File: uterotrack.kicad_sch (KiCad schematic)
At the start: 77 parts, among them J1 RFShield, J2 MicroSD_Card, J3 Argos_Prog, J4 AS5510, J5 Prog, J6 EXP, Q1 DMP2110UW, Q10 MMBT2222, Q11 MMBT2222, Q12 MMBT2222, Q13 MMBT2222, Q2 DMP2110UW, Q3 MMBT2222, Q4 DMP2110UW, Q5 DMP2110UW, Q6 MMBT2222, Q7 SiS415DNT, Q8 DMP2110UW, Q9 MMBT2222, U1 Argos_SMD, U2 ESP32-S3-WROOM-1, U3 keller_6LHPD, U4 RV-3032-C7, U5 CAM-M8Q

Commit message: Change R38, R39, R43 and R44 to 0402
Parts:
- R15, R16, R17, R23, R24, R26, R27, R28, R30, R31, R32, R33, R34, R36, R37: manf# CRCW0402100KFKEDC -> CRCW0402100KFKED
- R19, R20, R21, R22, R25: manf# CRCW04024K70FKEDC -> CRCW04024K70FKED
- R29, R35: manf# CRCW040220K0FKEDC -> CRCW040220K0FKED
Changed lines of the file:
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@@
 			)
 		)
-		(property "manf#" "CRCW0402100KFKEDC"
+		(property "manf#" "CRCW0402100KFKED"
 			(at 64.77 246.38 0)
 			(effects
@@
 			)
 		)
-		(property "manf#" "CRCW0402100KFKEDC"
+		(property "manf#" "CRCW0402100KFKED"
 			(at 87.63 167.64 0)
 			(effects
@@
 			)
 		)
-		(property "manf#" "CRCW0402100KFKEDC"
+		(property "manf#" "CRCW0402100KFKED"
 			(at 83.82 156.21 0)
 			(effects
@@
 			)
 		)
-		(property "manf#" "CRCW0402100KFKEDC"
+		(property "manf#" "CRCW0402100KFKED"
 			(at 121.92 234.95 0)
 			(effects
@@
 			)
 		)
-		(property "manf#" "CRCW04024K70FKEDC"
+		(property "manf#" "CRCW04024K70FKED"
 			(at 62.23 157.48 0)
 			(effects
@@
 			)
 		)
-		(property "manf#" "CRCW040220K0FKEDC"
+		(property "manf#" "CRCW040220K0FKED"
 			(at 106.68 247.65 0)
 			(effects
@@
 			)
 		)
-		(property "manf#" "CRCW0402100KFKEDC"
+		(property "manf#" "CRCW0402100KFKED"
 			(at 93.98 173.99 0)
 			(effects
@@
 			)
 		)
-		(property "manf#" "CRCW04024K70FKEDC"
+		(property "manf#" "CRCW04024K70FKED"
 			(at 62.23 154.94 0)
 			(effects
@@
 			)
 		)
-		(property "manf#" "CRCW0402100KFKEDC"
+		(property "manf#" "CRCW0402100KFKED"
 			(at 60.96 234.95 0)
 			(effects
@@
 			)
 		)
-		(property "manf#" "CRCW0402100KFKEDC"
+		(property "manf#" "CRCW0402100KFKED"
 			(at 196.85 259.08 0)
 			(effects
@@
 			)
 		)
-		(property "manf#" "CRCW0402100KFKEDC"
+		(property "manf#" "CRCW0402100KFKED"
 			(at 125.73 246.38 0)
 			(effects
@@
 			)
 		)
-		(property "manf#" "CRCW0402100KFKEDC"
+		(property "manf#" "CRCW0402100KFKED"
 			(at 290.83 83.82 0)
 			(effects
@@
 			)
 		)
-		(property "manf#" "CRCW04024K70FKEDC"
+		(property "manf#" "CRCW04024K70FKED"
 			(at 105.41 111.76 0)
 			(effects
@@
 			)
 		)
-		(property "manf#" "CRCW0402100KFKEDC"
+		(property "manf#" "CRCW0402100KFKED"
 			(at 294.64 72.39 0)
 			(effects
@@
 			)
 		)
-		(property "manf#" "CRCW0402100KFKEDC"
+		(property "manf#" "CRCW0402100KFKED"
 			(at 129.54 156.21 0)
 			(effects
@@
 			)
 		)
-		(property "manf#" "CRCW0402100KFKEDC"
+		(property "manf#" "CRCW0402100KFKED"
 			(at 48.26 74.93 0)
 			(effects
@@
 			)
 		)
-		(property "manf#" "CRCW0402100KFKEDC"
+		(property "manf#" "CRCW0402100KFKED"
 			(at 71.12 252.73 0)
 			(effects
@@
 			)
 		)
-		(property "manf#" "CRCW04024K70FKEDC"
+		(property "manf#" "CRCW04024K70FKED"
 			(at 49.53 111.76 0)
 			(effects
@@
 			)
 		)
-		(property "manf#" "CRCW0402100KFKEDC"
+		(property "manf#" "CRCW0402100KFKED"
 			(at 201.93 243.84 0)
 			(effects
@@
 			)
 		)
-		(property "manf#" "CRCW040220K0FKEDC"
+		(property "manf#" "CRCW040220K0FKED"
 			(at 106.68 234.95 0)
 			(effects
@@
 			)
 		)
-		(property "manf#" "CRCW04024K70FKEDC"
+		(property "manf#" "CRCW04024K70FKED"
 			(at 49.53 109.22 0)
 			(effects
@@
 			)
 		)
-		(property "manf#" "CRCW0402100KFKEDC"
+		(property "manf#" "CRCW0402100KFKED"
 			(at 168.91 246.38 0)
 			(effects

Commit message: Change resistor of uSD and Argus PA to 0402
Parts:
- C4: footprint Capacitor_SMD:C_0603_1608Metric -> Capacitor_SMD:C_0402_1005Metric; manf# 0603YC104JAT2A -> CL05B104KO5NNNC
- R1, R2, R3, R4, R5, R8: footprint Resistor_SMD:R_0603_1608Metric -> Resistor_SMD:R_0402_1005Metric; manf# CRCW06030000Z0EAC -> CRCW04020000Z0ED
- R10, R11, R12, R13, R14, R18, R6, R7, R9: footprint Resistor_SMD:R_0603_1608Metric -> Resistor_SMD:R_0402_1005Metric; manf# CRCW060310K0FKEAC -> CRCW040210K0FKED
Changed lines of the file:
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@@
 			)
 		)
-		(property "Footprint" "Resistor_SMD:R_0603_1608Metric"
+		(property "Footprint" "Resistor_SMD:R_0402_1005Metric"
 			(at 85.09 103.378 90)
 			(effects
@@
 			)
 		)
-		(property "manf#" "CRCW060310K0FKEAC"
+		(property "manf#" "CRCW040210K0FKED"
 			(at 85.09 101.6 0)
 			(effects
@@
 			)
 		)
-		(property "Footprint" "Resistor_SMD:R_0603_1608Metric"
+		(property "Footprint" "Resistor_SMD:R_0402_1005Metric"
 			(at 64.262 62.23 90)
 			(effects
@@
 			)
 		)
-		(property "manf#" "CRCW060310K0FKEAC"
+		(property "manf#" "CRCW040210K0FKED"
 			(at 66.04 62.23 0)
 			(effects
@@
 			)
 		)
-		(property "Footprint" "Resistor_SMD:R_0603_1608Metric"
+		(property "Footprint" "Resistor_SMD:R_0402_1005Metric"
 			(at 57.15 50.038 90)
 			(effects
@@
 			)
 		)
-		(property "manf#" "CRCW06030000Z0EAC"
+		(property "manf#" "CRCW04020000Z0ED"
 			(at 57.15 48.26 0)
 			(effects
@@
 			)
 		)
-		(property "Footprint" "Resistor_SMD:R_0603_1608Metric"
+		(property "Footprint" "Resistor_SMD:R_0402_1005Metric"
 			(at 66.802 62.23 90)
 			(effects
@@
 			)
 		)
-		(property "manf#" "CRCW060310K0FKEAC"
+		(property "manf#" "CRCW040210K0FKED"
 			(at 68.58 62.23 0)
 			(effects
@@
 			)
 		)
-		(property "Footprint" "Resistor_SMD:R_0603_1608Metric"
+		(property "Footprint" "Resistor_SMD:R_0402_1005Metric"
 			(at 74.422 62.23 90)
 			(effects
@@
 			)
 		)
-		(property "manf#" "CRCW060310K0FKEAC"
+		(property "manf#" "CRCW040210K0FKED"
 			(at 76.2 62.23 0)
 			(effects
@@
 			)
 		)
-		(property "Footprint" "Resistor_SMD:R_0603_1608Metric"
+		(property "Footprint" "Resistor_SMD:R_0402_1005Metric"
 			(at 57.15 42.418 90)
 			(effects
@@
 			)
 		)
-		(property "manf#" "CRCW06030000Z0EAC"
+		(property "manf#" "CRCW04020000Z0ED"
 			(at 57.15 40.64 0)
 			(effects
@@
 			)
 		)
-		(property "Footprint" "Resistor_SMD:R_0603_1608Metric"
+		(property "Footprint" "Resistor_SMD:R_0402_1005Metric"
 			(at 57.15 57.658 90)
 			(effects
@@
 			)
 		)
-		(property "manf#" "CRCW06030000Z0EAC"
+		(property "manf#" "CRCW04020000Z0ED"
 			(at 57.15 55.88 0)
 			(effects
@@
 			)
 		)
-		(property "Footprint" "Resistor_SMD:R_0603_1608Metric"
+		(property "Footprint" "Resistor_SMD:R_0402_1005Metric"
 			(at 69.342 62.23 90)
 			(effects
@@
 			)
 		)
-		(property "manf#" "CRCW060310K0FKEAC"
+		(property "manf#" "CRCW040210K0FKED"
 			(at 71.12 62.23 0)
 			(effects
@@
 			)
 		)
-		(property "Footprint" "Resistor_SMD:R_0603_1608Metric"
+		(property "Footprint" "Resistor_SMD:R_0402_1005Metric"
 			(at 220.218 54.61 90)
 			(effects
@@
 			)
 		)
-		(property "manf#" "CRCW060310K0FKEAC"
+		(property "manf#" "CRCW040210K0FKED"
 			(at 218.44 54.61 0)
 			(effects
@@
 			)
 		)
-		(property "Footprint" "Resistor_SMD:R_0603_1608Metric"
+		(property "Footprint" "Resistor_SMD:R_0402_1005Metric"
 			(at 57.15 44.958 90)
 			(effects
@@
 			)
 		)
-		(property "manf#" "CRCW06030000Z0EAC"
+		(property "manf#" "CRCW04020000Z0ED"
 			(at 57.15 43.18 0)
 			(effects
@@
 			)
 		)
-		(property "Footprint" "Resistor_SMD:R_0603_1608Metric"
+		(property "Footprint" "Resistor_SMD:R_0402_1005Metric"
 			(at 57.15 39.878 90)
 			(effects
@@
 			)
 		)
-		(property "manf#" "CRCW06030000Z0EAC"
+		(property "manf#" "CRCW04020000Z0ED"
 			(at 57.15 38.1 0)
 			(effects
@@
 			)
 		)
-		(property "Footprint" "Resistor_SMD:R_0603_1608Metric"
+		(property "Footprint" "Resistor_SMD:R_0402_1005Metric"
 			(at 242.062 54.61 90)
 			(effects
@@
 			)
 		)
-		(property "manf#" "CRCW060310K0FKEAC"
+		(property "manf#" "CRCW040210K0FKED"
 			(at 243.84 54.61 0)
 			(effects
@@
 			)
 		)
-		(property "Footprint" "Capacitor_SMD:C_0603_1608Metric"
+		(property "Footprint" "Capacitor_SMD:C_0402_1005Metric"
 			(at 82.2452 68.58 0)
 			(effects
@@
 			)
 		)
-		(property "manf#" "0603YC104JAT2A"
+		(property "manf#" "CL05B104KO5NNNC"
 			(at 81.28 72.39 0)
 			(effects
@@
 			)
 		)
-		(property "Footprint" "Resistor_SMD:R_0603_1608Metric"
+		(property "Footprint" "Resistor_SMD:R_0402_1005Metric"
 			(at 61.722 62.23 90)
 			(effects
@@
 			)
 		)
-		(property "manf#" "CRCW060310K0FKEAC"
+		(property "manf#" "CRCW040210K0FKED"
 			(at 63.5 62.23 0)
 			(effects
@@
 			)
 		)
-		(property "Footprint" "Resistor_SMD:R_0603_1608Metric"
+		(property "Footprint" "Resistor_SMD:R_0402_1005Metric"
 			(at 71.882 62.23 90)
 			(effects
@@
 			)
 		)
-		(property "manf#" "CRCW060310K0FKEAC"
+		(property "manf#" "CRCW040210K0FKED"
 			(at 73.66 62.23 0)
 			(effects
@@
 			)
 		)
-		(property "Footprint" "Resistor_SMD:R_0603_1608Metric"
+		(property "Footprint" "Resistor_SMD:R_0402_1005Metric"
 			(at 57.15 55.118 90)
 			(effects
@@
 			)
 		)
-		(property "manf#" "CRCW06030000Z0EAC"
+		(property "manf#" "CRCW04020000Z0ED"
 			(at 57.15 53.34 0)
 			(effects

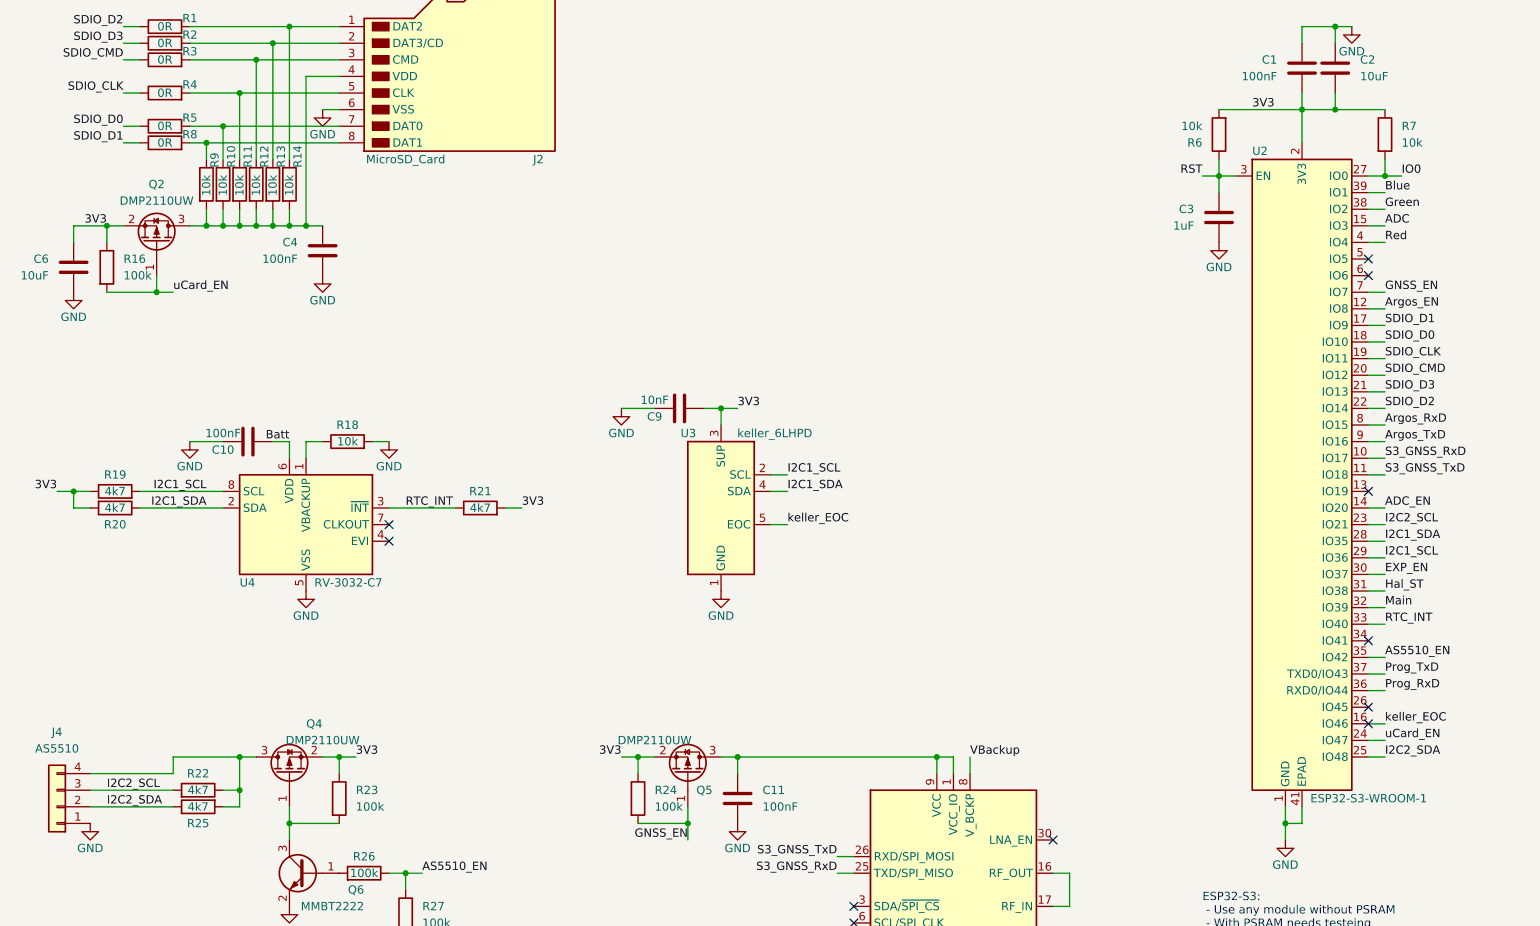
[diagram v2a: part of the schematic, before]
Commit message: Swap I2C_1 with I2C_2 and rename R6 to R8
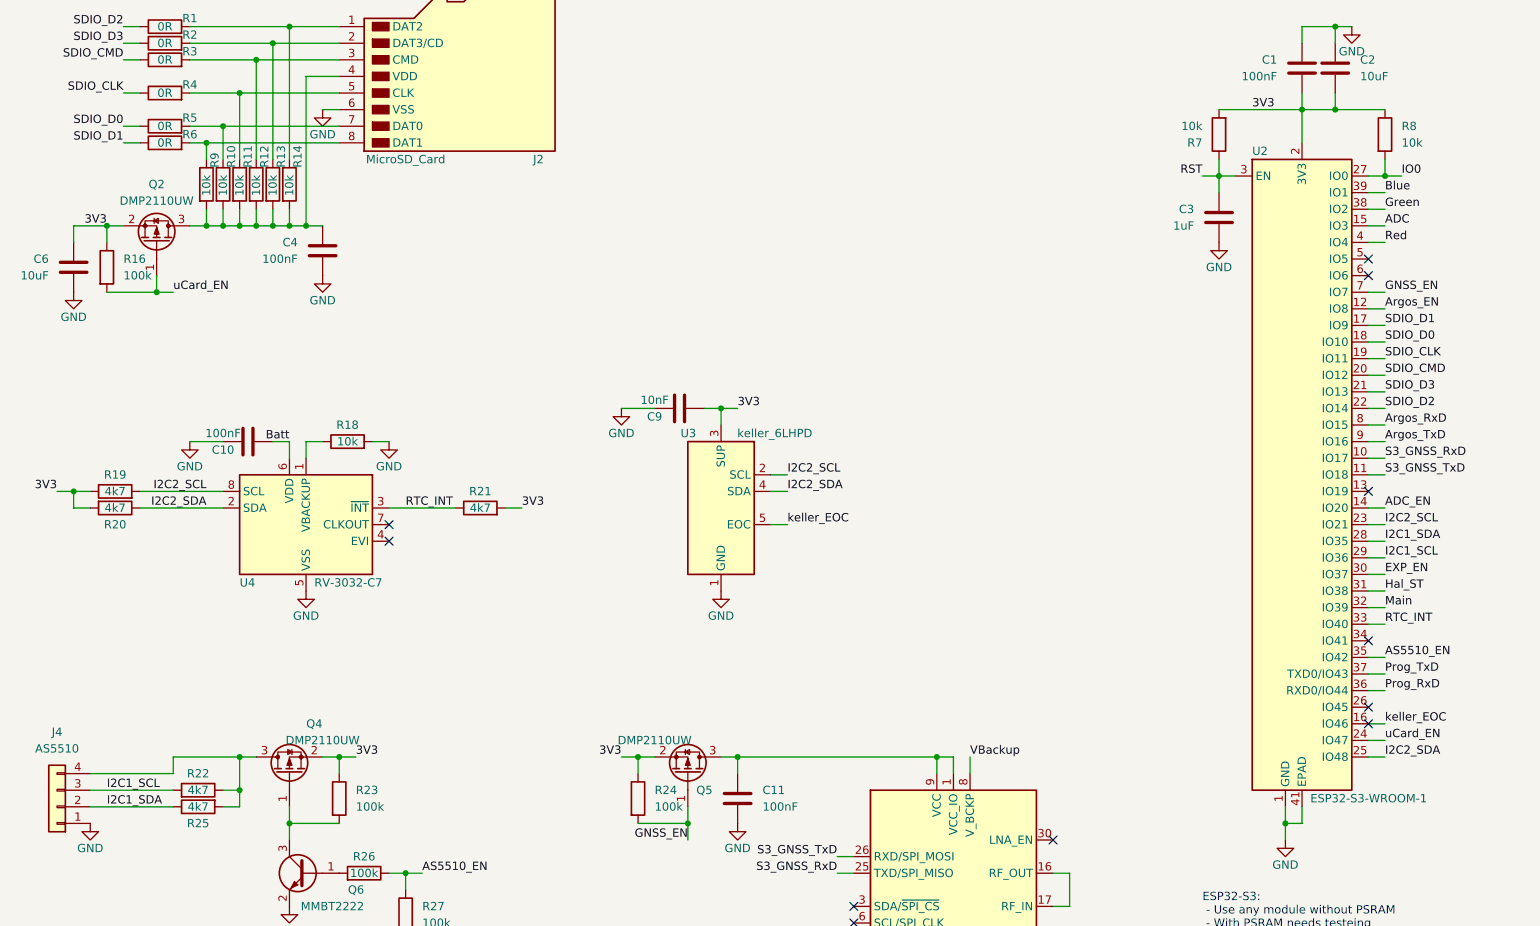
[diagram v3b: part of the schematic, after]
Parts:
- renumbered R8 to R6, R6 to R7, R7 to R8
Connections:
- net I2C1_SCL: now also J4.3 (Pin_3), R22.2; no longer R19.2, U3.2 (SCL), U4.8 (SCL)
- net I2C1_SDA: now also J4.2 (Pin_2), R25.1; no longer R20.1, U3.4 (SDA), U4.2 (SDA)
- net I2C2_SCL: now also R19.2, U3.2 (SCL), U4.8 (SCL); no longer J4.3 (Pin_3), R22.2
- net I2C2_SDA: now also R20.1, U3.4 (SDA), U4.2 (SDA); no longer J4.2 (Pin_2), R25.1
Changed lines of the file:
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@@
 		)
 	)
-	(label "I2C2_SCL"
+	(label "I2C1_SCL"
 		(at 48.26 154.94 0)
 		(effects
@@
 		)
 	)
-	(label "I2C2_SDA"
+	(label "I2C1_SDA"
 		(at 48.26 157.48 0)
 		(effects
@@
 		)
 	)
-	(label "I2C1_SCL"
+	(label "I2C2_SCL"
 		(at 63.5 109.22 180)
 		(effects
@@
 		)
 	)
-	(label "I2C1_SCL"
+	(label "I2C2_SCL"
 		(at 152.4 106.68 0)
 		(effects
@@
 		)
 	)
-	(label "I2C1_SDA"
+	(label "I2C2_SDA"
 		(at 63.5 111.76 180)
 		(effects
@@
 		)
 	)
-	(label "I2C1_SDA"
+	(label "I2C2_SDA"
 		(at 152.4 109.22 0)
 		(effects
@@
 		(on_board yes)
 		(dnp no)
-		(property "Reference" "R8"
+		(property "Reference" "R6"
 			(at 60.96 54.61 90)
 			(effects
@@
 			(project "uterotrack"
 				(path "/02cd0949-8d8d-4522-9baa-94804311f80f"
-					(reference "R8")
+					(reference "R6")
 					(unit 1)
 				)
@@
 		(on_board yes)
 		(dnp no)
-		(property "Reference" "R6"
+		(property "Reference" "R7"
 			(at 215.9 55.8801 0)
 			(effects
@@
 			(project "uterotrack"
 				(path "/02cd0949-8d8d-4522-9baa-94804311f80f"
-					(reference "R6")
+					(reference "R7")
 					(unit 1)
 				)
@@
 		(on_board yes)
 		(dnp no)
-		(property "Reference" "R7"
+		(property "Reference" "R8"
 			(at 246.38 53.3399 0)
 			(effects
@@
 			(project "uterotrack"
 				(path "/02cd0949-8d8d-4522-9baa-94804311f80f"
-					(reference "R7")
+					(reference "R8")
 					(unit 1)
 				)

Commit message: Add first version of PCB
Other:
- title: Trident V3 -> UteroTrack
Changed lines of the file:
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@@
 	(paper "A3")
 	(title_block
-		(title "Trident V3")
-		(rev "1.0.1")
+		(title "UteroTrack")
+		(rev "1.0.0")
 		(company "ElectricBlue")
+		(comment 1 "JNeiva")
 	)
 	(text "ESP32-S3:\n - Use any module without PSRAM\n - With PSRAM needs testeing\n - Incompatible With PSRAM Octal SPI,\n	pins already in use"
